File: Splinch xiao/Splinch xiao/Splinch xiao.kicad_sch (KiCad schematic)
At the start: 0 parts

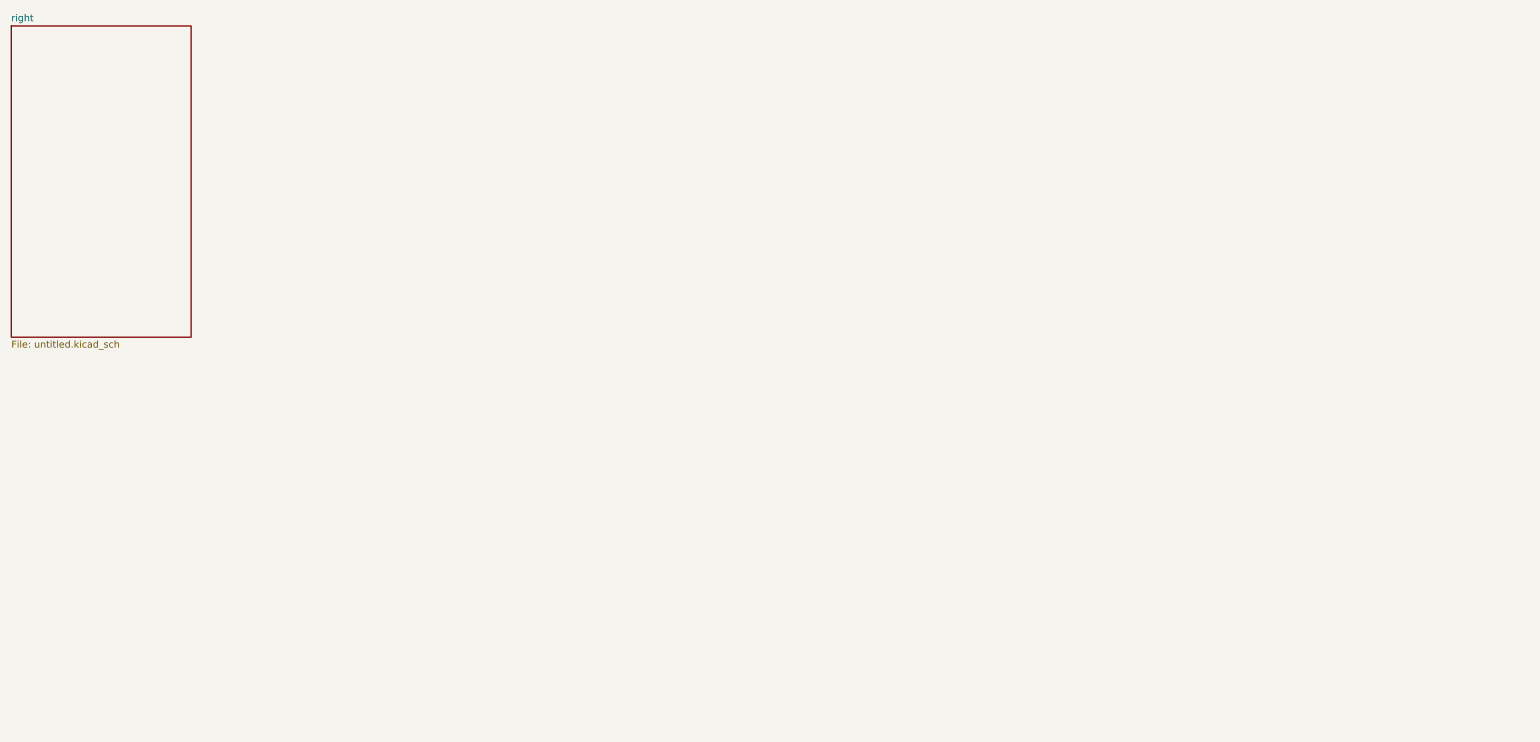
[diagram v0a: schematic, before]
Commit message: outline and left schem
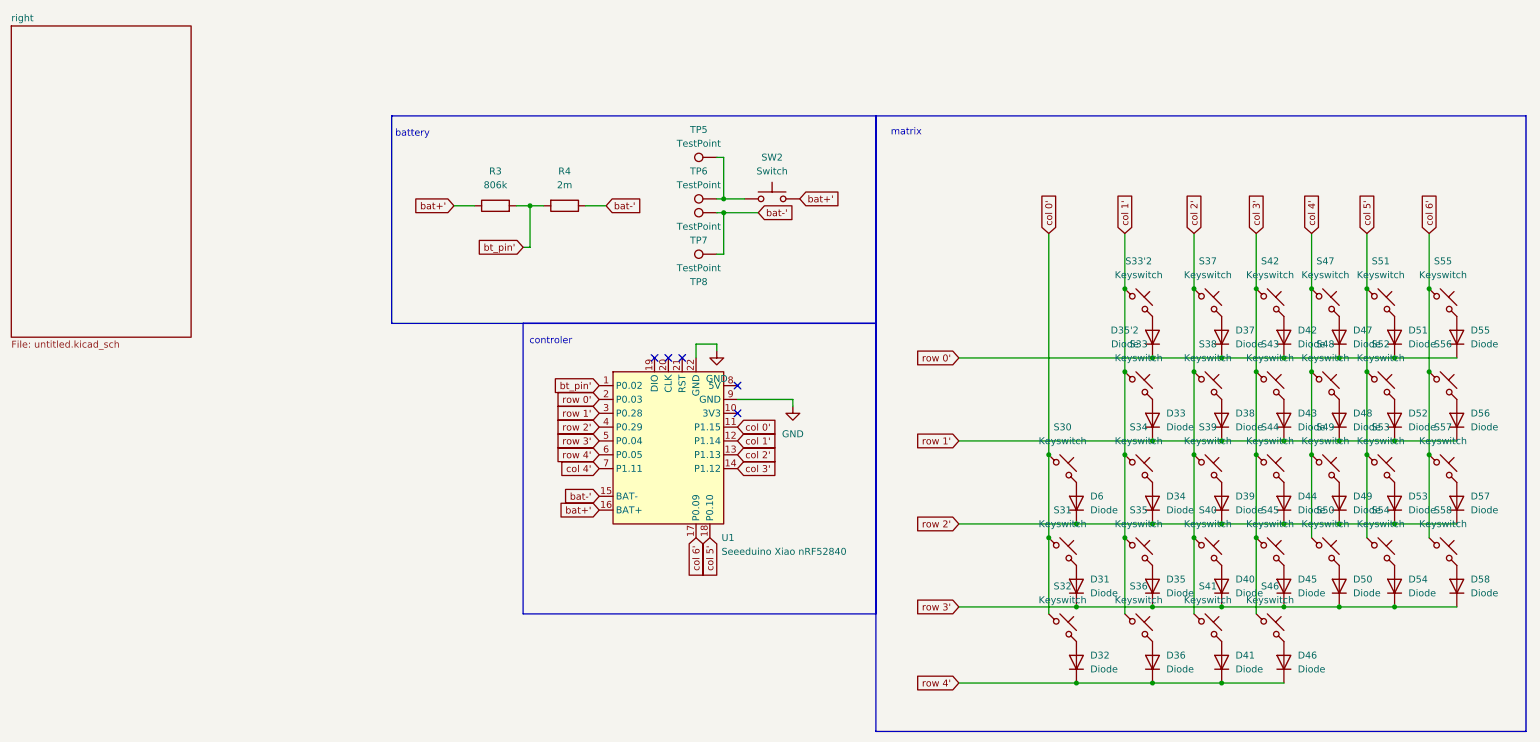
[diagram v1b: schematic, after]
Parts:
- added D31, D32, D33, D34, D35, D35'2, D36, D37, D38, D39, D40, D41, D42, D43, D44, D45, D46, D47, D48, D49, D50, D51, D52, D53, D54, D55, D56, D57, D58, D6: Diode, ScottoKeebs_Components:Diode_SOD-123, symbol ScottoKeebs:Placeholder_Diode
- added R3: 806k, Resistor_SMD:R_0805_2012Metric_Pad1.20x1.40mm_HandSolder, symbol Device:R
- added R4: 2m, Resistor_SMD:R_0805_2012Metric_Pad1.20x1.40mm_HandSolder, symbol Device:R
- added S30, S31, S32, S33, S33'2, S34, S35, S36, S37, S38, S39, S40, S41, S42, S43, S44, S45, S46, S47, S48, S49, S50, S51, S52, S53, S54, S55, S56, S57, S58: Keyswitch, keyswitches.pretty-master:Kailh_socket_PG1350, symbol ScottoKeebs:Placeholder_Keyswitch
- added SW2: Switch, ScottoKeebs_Components:Switch_MSK12C02, symbol ScottoKeebs:Placeholder_Switch
- added TP5, TP6, TP7, TP8: TestPoint, TestPoint:TestPoint_Pad_D3.0mm, symbol Connector:TestPoint
- added U1: Seeeduino Xiao nRF52840, marbastlib-xp-promicroish:Xiao_nRF52840_ACH, symbol marbastlib-promicroish:Seeeduino_Xiao_nRF52840
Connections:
- new net: D37.2 (A), S37.2
- new net: D40.2 (A), S40.2
- new net: D52.2 (A), S52.2
- new net: D43.2 (A), S43.2
- new net: D48.2 (A), S48.2
- new net: D53.2 (A), S53.2
- new net: D41.2 (A), S41.2
- new net: D36.2 (A), S36.2
- new net: D34.2 (A), S34.2
- new net: D49.2 (A), S49.2
- new net: D51.2 (A), S51.2
- new net: SW2.2, TP5.1, TP6.1
- new net: D31.2 (A), S31.2
- new net: D50.2 (A), S50.2
- new net: D39.2 (A), S39.2
- new net: D35'2.2 (A), S33'2.2
- new net: D32.2 (A), S32.2
- new net: D47.2 (A), S47.2
- new net: D56.2 (A), S56.2
- new net: D46.2 (A), S46.2
- new net: D35.2 (A), S35.2
- new net: D44.2 (A), S44.2
- new net: D58.2 (A), S58.2
- new net: D38.2 (A), S38.2
- new net: D6.2 (A), S30.2
- new net: D54.2 (A), S54.2
- new net: D42.2 (A), S42.2
- new net: D55.2 (A), S55.2
- new net: D33.2 (A), S33.2
- new net: D45.2 (A), S45.2
- new net: D57.2 (A), S57.2
- new net GND: U1.22 (GND), U1.9 (GND)
- new net bat+': R3.1, SW2.1, U1.16 (BAT+)
- new net bat-': R4.1, TP7.1, TP8.1, U1.15 (BAT-)
- new net bt_pin': R3.2, R4.2, U1.1 (P0.02)
- new net col 0': S30.1, S31.1, S32.1, U1.11 (P1.15)
- new net col 1': S33'2.1, S33.1, S34.1, S35.1, S36.1, U1.12 (P1.14)
- new net col 2': S37.1, S38.1, S39.1, S40.1, S41.1, U1.13 (P1.13)
- new net col 3': S42.1, S43.1, S44.1, S45.1, S46.1, U1.14 (P1.12)
- new net col 4': S47.1, S48.1, S49.1, S50.1, U1.7 (P1.11)
- new net col 5': S51.1, S52.1, S53.1, S54.1, U1.18 (P0.10)
- new net col 6': S55.1, S56.1, S57.1, S58.1, U1.17 (P0.09)
- new net row 0': D35'2.1 (K), D37.1 (K), D42.1 (K), D47.1 (K), D51.1 (K), D55.1 (K), U1.2 (P0.03)
- new net row 1': D33.1 (K), D38.1 (K), D43.1 (K), D48.1 (K), D52.1 (K), D56.1 (K), U1.3 (P0.28)
- new net row 2': D34.1 (K), D39.1 (K), D44.1 (K), D49.1 (K), D53.1 (K), D57.1 (K), D6.1 (K), U1.4 (P0.29)
- new net row 3': D31.1 (K), D35.1 (K), D40.1 (K), D45.1 (K), D50.1 (K), D54.1 (K), D58.1 (K), U1.5 (P0.04)
- new net row 4': D32.1 (K), D36.1 (K), D41.1 (K), D46.1 (K), U1.6 (P0.05)
- no-connect marks 0 -> 5
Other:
- note added: "battery"
- note added: "controler"
- note added: "matrix"

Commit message: did some of the other galf
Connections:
- net GND: no longer U1.9 (GND)
- new net GND': U1.9 (GND)
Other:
- moved on the sheet: D31, D32, D33, D34, D35, D35'2, D36, D37, D38, D39, D40, D41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

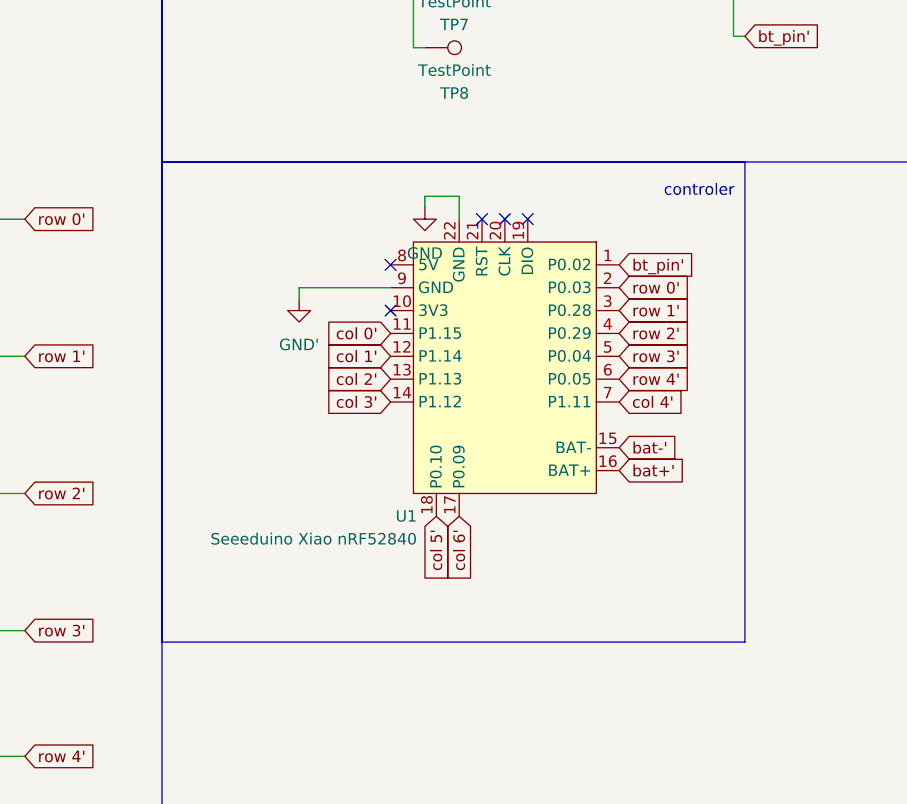
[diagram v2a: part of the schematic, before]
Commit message: case' wiring and more
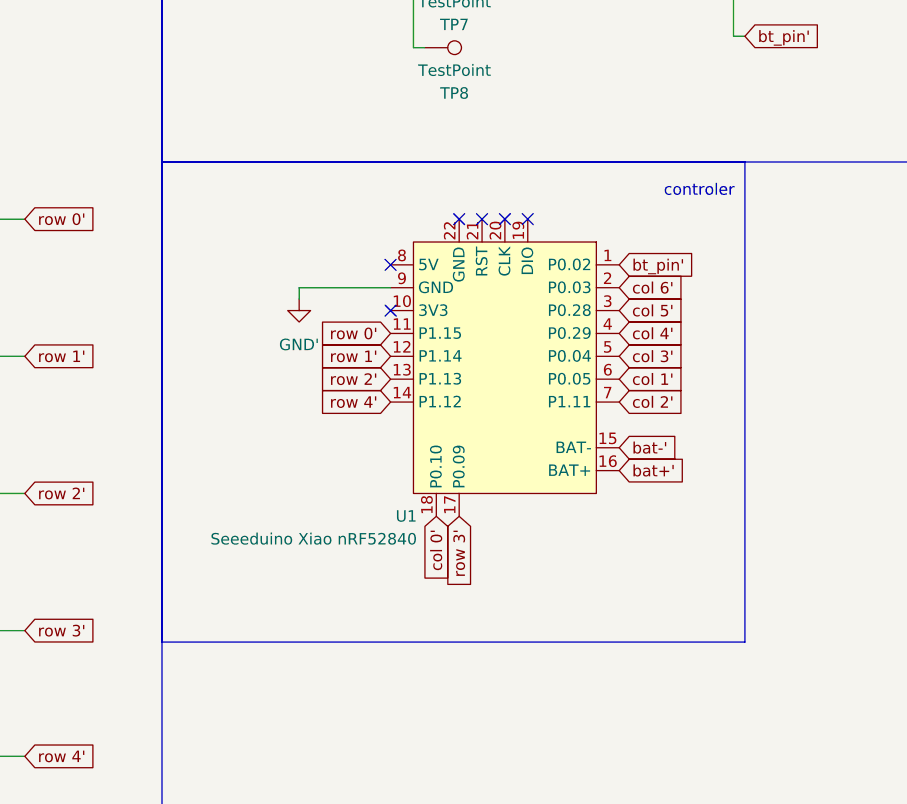
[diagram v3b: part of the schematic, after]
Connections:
- net col 0': now also U1.18 (P0.10); no longer U1.11 (P1.15)
- net col 1': now also U1.6 (P0.05); no longer U1.12 (P1.14)
- net col 2': now also U1.7 (P1.11); no longer U1.13 (P1.13)
- net col 3': now also U1.5 (P0.04); no longer U1.14 (P1.12)
- net col 4': now also U1.4 (P0.29); no longer U1.7 (P1.11)
- net col 5': now also U1.3 (P0.28); no longer U1.18 (P0.10)
- net col 6': now also U1.2 (P0.03); no longer U1.17 (P0.09)
- net row 0': now also U1.11 (P1.15); no longer U1.2 (P0.03)
- net row 1': now also U1.12 (P1.14); no longer U1.3 (P0.28)
- net row 2': now also U1.13 (P1.13); no longer U1.4 (P0.29)
- net row 3': now also U1.17 (P0.09); no longer U1.5 (P0.04)
- net row 4': now also U1.14 (P1.12); no longer U1.6 (P0.05)
- net GND: no longer names the net of U1.22 (GND)
- no-connect marks 5 -> 6

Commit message: added silk screen and reade me
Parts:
- D31, D32, D33, D34, D35, D35'2, D36, D37, D38, D39, D40, D41, D42, D43, D44, D45, D46, D47, D48, D49, D50, D51, D52, D53, D54, D55, D56, D57, D58, D6: LCSC (none) -> C2128
- R3: LCSC (none) -> C121025
- R4: value 2m -> 2M; LCSC (none) -> C106170
